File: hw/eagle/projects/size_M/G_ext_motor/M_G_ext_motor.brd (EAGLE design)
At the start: 11 parts, among them IC1 AT414, X22 A1250WR

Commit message: pcb M.1 -not finished
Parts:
- removed C1: 100n, rcl:C0603
- removed JP2: (no value), pinhead2:1X06
- removed JP3: (no value), pinhead2:1X05
- added G.C1: 100n, rcl:C0603
- added G.J1: (no value), pinhead2:1X06
- added G.J2: (no value), pinhead2:1X05
- renumbered C2 to G.C2, C3 to G.C3, C4 to G.C4, C5 to G.C5, IC1 to G.U1, MX1 to G.U2, U$1 to G.MOTO1, X22 to G.J3
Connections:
- net GND: now also G.J1.6, G.J2.3; no longer JP2.6, JP3.3
- net M3: now also G.C1.2; no longer C1.2
- net M4: now also G.C1.1; no longer C1.1
- net M_SRC: now also G.J2.1; no longer JP3.1
- net N$19: now also G.J1.1; no longer JP2.1
- net N$20: now also G.J1.2; no longer JP2.2
- net N$7: now also G.J2.5; no longer JP3.5
- net VCC: now also G.J2.4; no longer JP3.4
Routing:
- net M_SRC: track 15.7 -> 13.4 mm
- net GND: track 87.7 -> 88.4 mm
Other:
- board text added: "1"
- board text added: "2"
- board text added: "moto M.1"
- board text removed: "moto M.0"

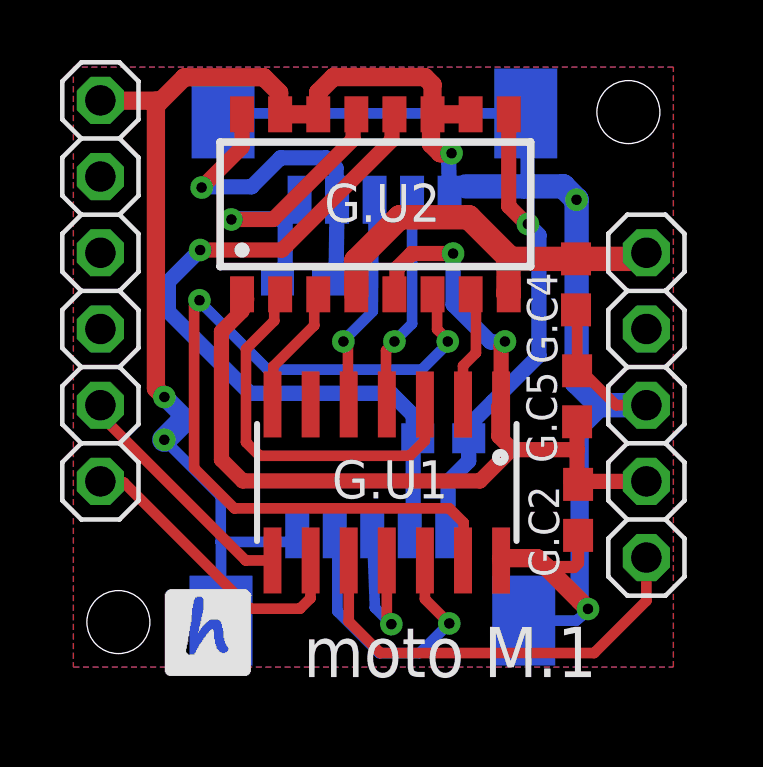
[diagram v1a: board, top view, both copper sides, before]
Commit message: updateed PCBs - adjustments based on usage of version 1
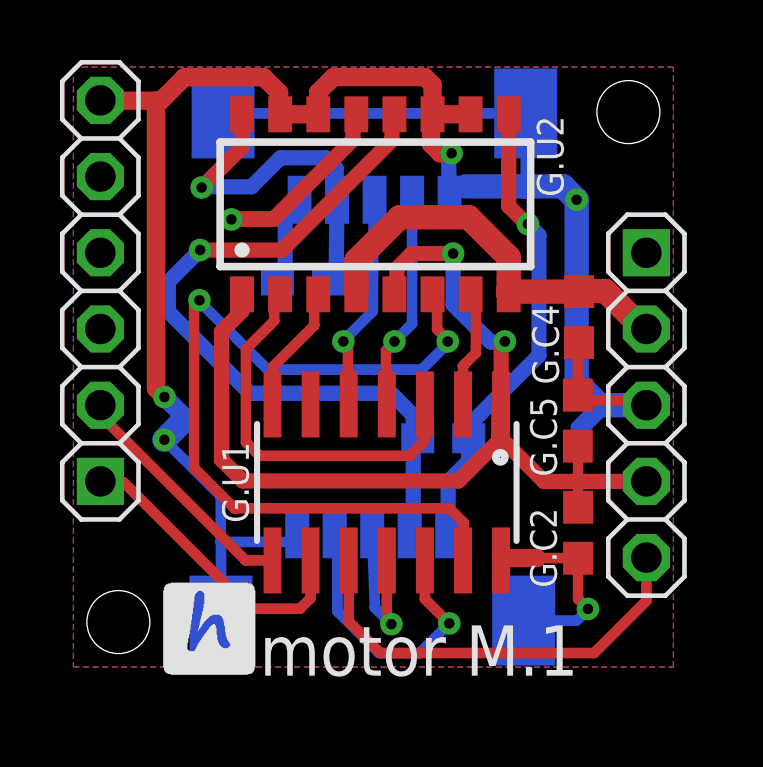
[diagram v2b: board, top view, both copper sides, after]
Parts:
- moved G.C4 1.10 mm to (17.4, 12.2)
- moved G.C5 0.81 mm to (17.3, 8.71)
- moved G.C2 0.76 mm to (17.3, 4.98)
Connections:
- net M_SRC: now also G.J2.2; no longer G.J2.1
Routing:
- net GND: track 88.4 -> 81.2 mm
- net M_SRC: track 13.4 -> 14.0 mm
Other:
- board text added: "motor M.1"
- board text removed: "moto M.1"
